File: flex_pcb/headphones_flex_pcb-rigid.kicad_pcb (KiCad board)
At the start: 2 copper layers, 41.7 x 25.7 mm, 34 parts, among them J1 LIGHTING_JACK, J2 CONN_01X01, J3 BOTTOM_FLEX_LIGHTNING, J5 LIGHTNING_HEADPHONE_ADAPTER, J7 IPHONE_HEADPHONE_JACK, U1 SN74LVC1G123, U2 SN74LVC1G123, U3 NC7S32-micropak6, U4 TS3Y5018RSV-UQFN

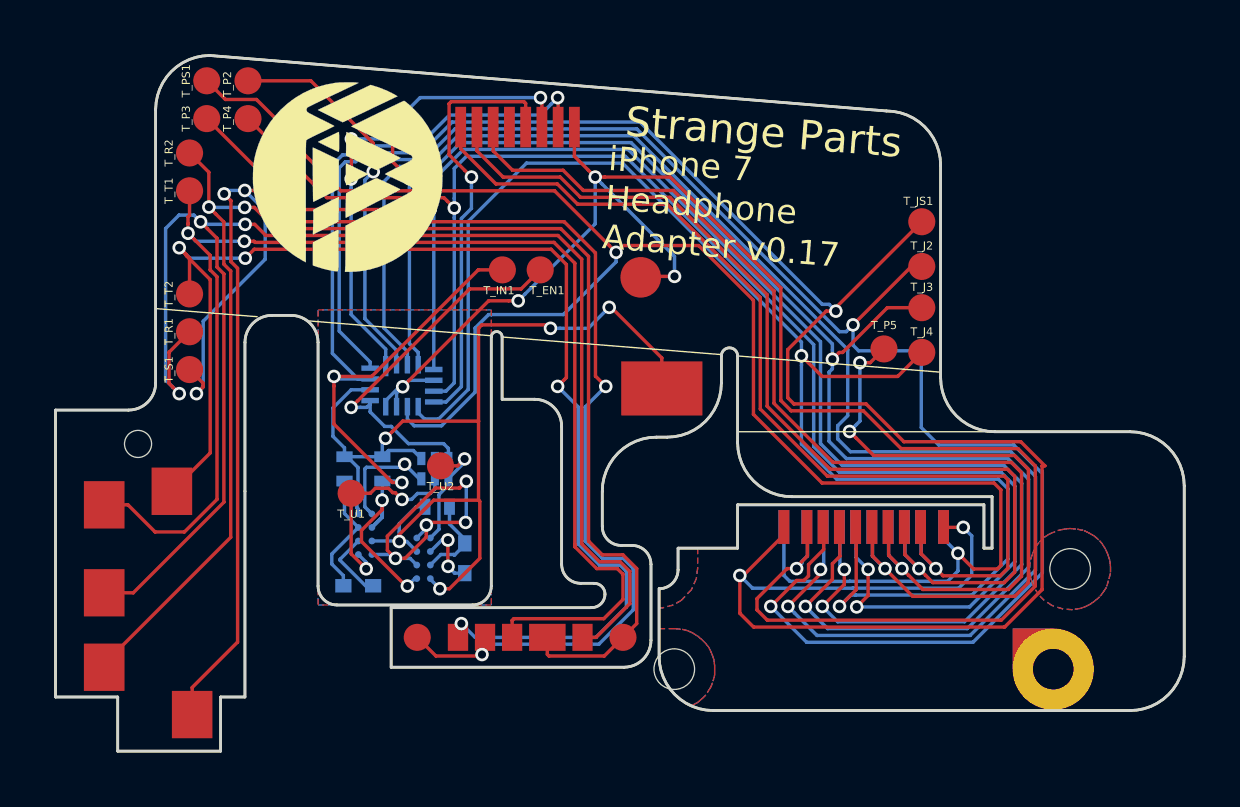
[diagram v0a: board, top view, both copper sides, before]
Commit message: v0.17
I redesigned the flex pcb to use the TS3A5018 chip
for switching instead of the ADG774A.  This supports
a 3v signal, whereas the ADG774A only supported up
to 1.5v.  Also a bunch of minor tweaks to the board
design to make it easier to assemble and test (added
test pads!)

Also made a rigid version of the flex pcb, to help
debug manufacturing defects if necessary.
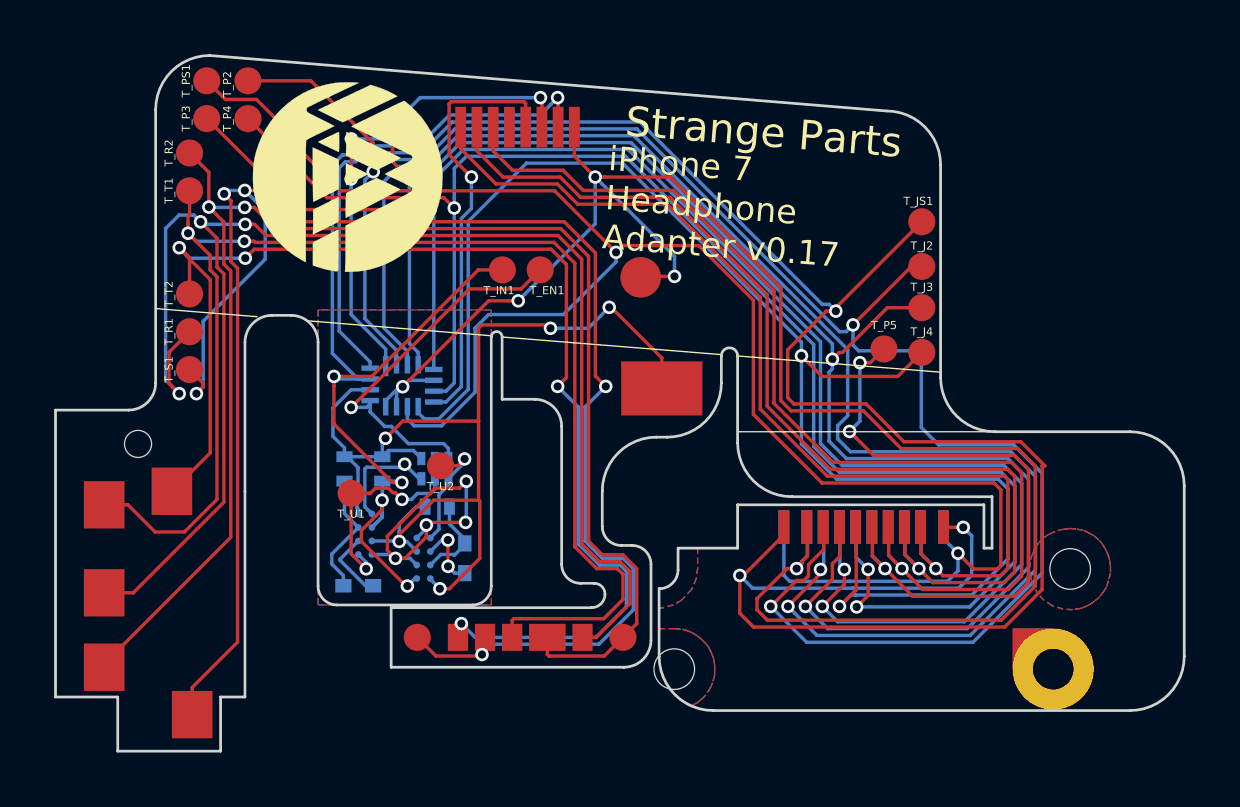
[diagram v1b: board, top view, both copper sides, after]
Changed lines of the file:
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@@
     (links 77)
     (no_connects 0)
-    (area 112.994999 60.749999 165.635707 92.201)
-    (thickness 0.2)
-    (drawings 149)
+    (area 122.749999 60.749999 164.550001 86.550001)
+    (thickness 1)
+    (drawings 84)
     (tracks 788)
     (zones 0)
@@
   )
   (layers
-    (0 F.Cu signal hide)
-    (31 B.Cu signal hide)
-    (32 B.Adhes user hide)
-    (33 F.Adhes user hide)
-    (34 B.Paste user hide)
-    (35 F.Paste user hide)
-    (36 B.SilkS user hide)
+    (0 F.Cu signal)
+    (31 B.Cu signal)
+    (32 B.Adhes user)
+    (33 F.Adhes user)
+    (34 B.Paste user)
+    (35 F.Paste user)
+    (36 B.SilkS user)
     (37 F.SilkS user)
-    (38 B.Mask user hide)
-    (39 F.Mask user hide)
-    (40 Dwgs.User user hide)
-    (41 Cmts.User user hide)
-    (42 Eco1.User user hide)
-    (43 Eco2.User user hide)
+    (38 B.Mask user)
+    (39 F.Mask user)
+    (40 Dwgs.User user)
+    (41 Cmts.User user)
+    (42 Eco1.User user)
+    (43 Eco2.User user)
     (44 Edge.Cuts user)
-    (45 Margin user hide)
-    (46 B.CrtYd user hide)
-    (47 F.CrtYd user hide)
-    (48 B.Fab user hide)
-    (49 F.Fab user hide)
+    (45 Margin user)
+    (46 B.CrtYd user)
+    (47 F.CrtYd user)
+    (48 B.Fab user)
+    (49 F.Fab user)
   )
   (setup
@@
       (layerselection 0x010f0_80000001)
       (usegerberextensions false)
-      (gerberprecision 5)
       (excludeedgelayer true)
       (linewidth 0.100000)
@@
   (gr_line (start 132.1 70.6) (end 138.85 71.15) (layer F.SilkS) (width 0.05))
   (gr_line (start 126.5 70.15) (end 130.25 70.45) (layer F.SilkS) (width 0.05))
-  (gr_arc (start 125.5 72.9) (end 126.5 72.9) (angle 90) (layer F.SilkS) (width 0.1))
-  (gr_arc (start 131.5 71.4) (end 131.5 70.4) (angle 90) (layer F.SilkS) (width 0.1))
-  (gr_arc (start 130.8 71.4) (end 129.8 71.4) (angle 90) (layer F.SilkS) (width 0.1))
-  (gr_arc (start 133.2 80.4) (end 133.2 81.1) (angle 90) (layer F.SilkS) (width 0.1))
-  (gr_line (start 128.9 84.5) (end 129.8 84.5) (layer F.SilkS) (width 0.1))
-  (gr_line (start 128.9 84.5) (end 128.9 86.5) (layer F.SilkS) (width 0.1))
-  (gr_line (start 125.1 84.5) (end 125.1 86.5) (layer F.SilkS) (width 0.1))
-  (gr_line (start 122.8 84.5) (end 125.1 84.5) (layer F.SilkS) (width 0.1))
-  (gr_line (start 130.8 70.4) (end 131.5 70.4) (layer F.SilkS) (width 0.1))
-  (gr_line (start 129.8 76.9) (end 129.8 71.4) (layer F.SilkS) (width 0.1))
-  (gr_line (start 129.8 76.9) (end 129.8 84.5) (layer F.SilkS) (width 0.1))
-  (gr_line (start 122.8 73.9) (end 125.5 73.9) (layer F.SilkS) (width 0.1))
-  (gr_line (start 122.8 84.5) (end 122.8 73.9) (layer F.SilkS) (width 0.1))
-  (gr_line (start 128.9 86.5) (end 125.1 86.5) (layer F.SilkS) (width 0.1))
   (gr_line (start 157.5 74.7) (end 148 74.7) (layer Eco1.User) (width 0.01))
   (gr_line (start 155.448 72.517) (end 124.841 69.977) (angle 90) (layer Eco1.User) (width 0.01))
@@
     (effects (font (size 1.1 1.1) (thickness 0.18)))
   )
-  (gr_arc (start 150 75.1) (end 150 77.1) (angle 90) (layer F.SilkS) (width 0.1))
-  (gr_arc (start 140.5 74.5) (end 140.5 73.5) (angle 90) (layer F.SilkS) (width 0.1))
-  (gr_arc (start 142.7 80.7) (end 142.7 80.3) (angle 90) (layer F.SilkS) (width 0.1))
-  (gr_arc (start 142.2 79.6) (end 142.2 80.3) (angle 90) (layer F.SilkS) (width 0.1))
-  (gr_arc (start 143.7 78.2) (end 143.7 78.9) (angle 90) (layer F.SilkS) (width 0.1))
-  (gr_arc (start 144.1 79.6) (end 144.1 78.9) (angle 90) (layer F.SilkS) (width 0.1))
-  (gr_line (start 135.2 83.4) (end 135.2 81.2) (layer F.SilkS) (width 0.1))
-  (gr_line (start 139.3 73.5) (end 140.5 73.5) (layer F.SilkS) (width 0.1))
-  (gr_arc (start 145.1 79.8) (end 145.8 79.8) (angle 90) (layer F.SilkS) (width 0.1))
-  (gr_line (start 145.8 79) (end 145.8 79.8) (layer F.SilkS) (width 0.1))
-  (gr_line (start 145.8 79) (end 148 79) (layer F.SilkS) (width 0.1))
   (gr_circle (center 145.2 79.3) (end 145.9 79.3) (layer Eco2.User) (width 0.1))
-  (gr_line (start 141.5 79.6) (end 141.5 74.5) (layer F.SilkS) (width 0.1))
-  (gr_line (start 142.7 80.3) (end 142.2 80.3) (layer F.SilkS) (width 0.1))
-  (gr_line (start 144.1 78.9) (end 143.7 78.9) (layer F.SilkS) (width 0.1))
-  (gr_line (start 144.8 79.6) (end 144.8 82.4) (layer F.SilkS) (width 0.1))
-  (gr_arc (start 142.6 80.7) (end 143.1 80.7) (angle 90) (layer F.SilkS) (width 0.1))
-  (gr_line (start 135.2 81.2) (end 142.6 81.2) (layer F.SilkS) (width 0.1))
-  (gr_line (start 139.3 73.5) (end 139.3 71.2) (layer F.SilkS) (width 0.1))
-  (gr_line (start 143 78.2) (end 143 76.9) (layer F.SilkS) (width 0.1))
-  (gr_arc (start 145 76.9) (end 143 76.9) (angle 90) (layer F.SilkS) (width 0.1))
-  (gr_line (start 145.4 74.9) (end 145 74.9) (layer F.SilkS) (width 0.1))
-  (gr_arc (start 145.4 72.9) (end 147.4 72.9) (angle 90) (layer F.SilkS) (width 0.1))
-  (gr_line (start 147.4 72.9) (end 147.4 71.9) (layer F.SilkS) (width 0.1))
-  (gr_arc (start 147.7 71.9) (end 147.4 71.9) (angle 180) (layer F.SilkS) (width 0.1))
-  (gr_arc (start 139.1 71.2) (end 138.9 71.2) (angle 180) (layer F.SilkS) (width 0.1))
-  (gr_arc (start 138.2 80.4) (end 138.9 80.4) (angle 90) (layer F.SilkS) (width 0.1))
-  (gr_arc (start 143.8 82.4) (end 144.8 82.4) (angle 90) (layer F.SilkS) (width 0.1))
-  (gr_arc (start 128.5 62.8) (end 126.5 62.8) (angle 90) (layer F.SilkS) (width 0.1))
-  (gr_arc (start 153.5 64.85) (end 153.5 62.85) (angle 90) (layer F.SilkS) (width 0.1))
-  (gr_arc (start 147.1 83) (end 147.1 85) (angle 90) (layer F.SilkS) (width 0.1))
-  (gr_arc (start 162.5 83) (end 164.5 83) (angle 90) (layer F.SilkS) (width 0.1))
-  (gr_arc (start 162.5 76.7) (end 162.5 74.7) (angle 90) (layer F.SilkS) (width 0.1))
-  (gr_arc (start 157.5 72.7) (end 157.5 74.7) (angle 90) (layer F.SilkS) (width 0.1))
-  (gr_line (start 145.1 80.5) (end 145.1 83) (angle 90) (layer F.SilkS) (width 0.1))
-  (gr_line (start 143.8 83.4) (end 135.2 83.4) (layer F.SilkS) (width 0.1))
-  (gr_line (start 126.5 62.8) (end 126.5 72.9) (layer F.SilkS) (width 0.1))
-  (gr_line (start 153.5 62.85) (end 128.5 60.8) (layer F.SilkS) (width 0.1))
   (gr_line (start 157.5 72.7) (end 113 69) (layer Dwgs.User) (width 0.01))
-  (gr_line (start 138.2 81.1) (end 133.2 81.1) (layer F.SilkS) (width 0.1))
-  (gr_line (start 138.9 71.2) (end 138.9 80.4) (layer F.SilkS) (width 0.1))
-  (gr_line (start 157.1 77.4) (end 148 77.4) (angle 90) (layer F.SilkS) (width 0.1))
-  (gr_line (start 148 77.4) (end 148 79) (angle 90) (layer F.SilkS) (width 0.1))
-  (gr_line (start 132.5 71.4) (end 132.5 80.4) (angle 90) (layer F.SilkS) (width 0.1))
-  (gr_line (start 155.5 72.7) (end 155.5 64.85) (angle 90) (layer F.SilkS) (width 0.1))
-  (gr_line (start 148 71.9) (end 148 75.1) (angle 90) (layer F.SilkS) (width 0.1))
-  (gr_line (start 147.1 85) (end 162.5 85) (angle 90) (layer F.SilkS) (width 0.1))
-  (gr_line (start 164.5 83) (end 164.5 76.7) (angle 90) (layer F.SilkS) (width 0.1))
   (gr_line (start 157.5 74.7) (end 148 74.7) (angle 90) (layer Dwgs.User) (width 0.01))
-  (gr_line (start 157.4 77.1) (end 150 77.1) (angle 90) (layer F.SilkS) (width 0.1))
-  (gr_line (start 157.4 79) (end 157.4 77.1) (angle 90) (layer F.SilkS) (width 0.1))
-  (gr_line (start 157.1 79) (end 157.4 79) (angle 90) (layer F.SilkS) (width 0.1))
-  (gr_line (start 157.1 77.4) (end 157.1 79) (angle 90) (layer F.SilkS) (width 0.1))
-  (gr_line (start 157.5 74.7) (end 162.5 74.7) (angle 90) (layer F.SilkS) (width 0.1))
   (segment (start 133.008 79.587) (end 133.435 80.014) (width 0.127) (layer B.Cu) (net 1))
   (segment (start 133.008 79.217) (end 133.008 79.587) (width 0.127) (layer B.Cu) (net 1))
